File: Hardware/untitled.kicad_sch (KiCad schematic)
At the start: 3 parts, among them U1 STM32F446RET6TR

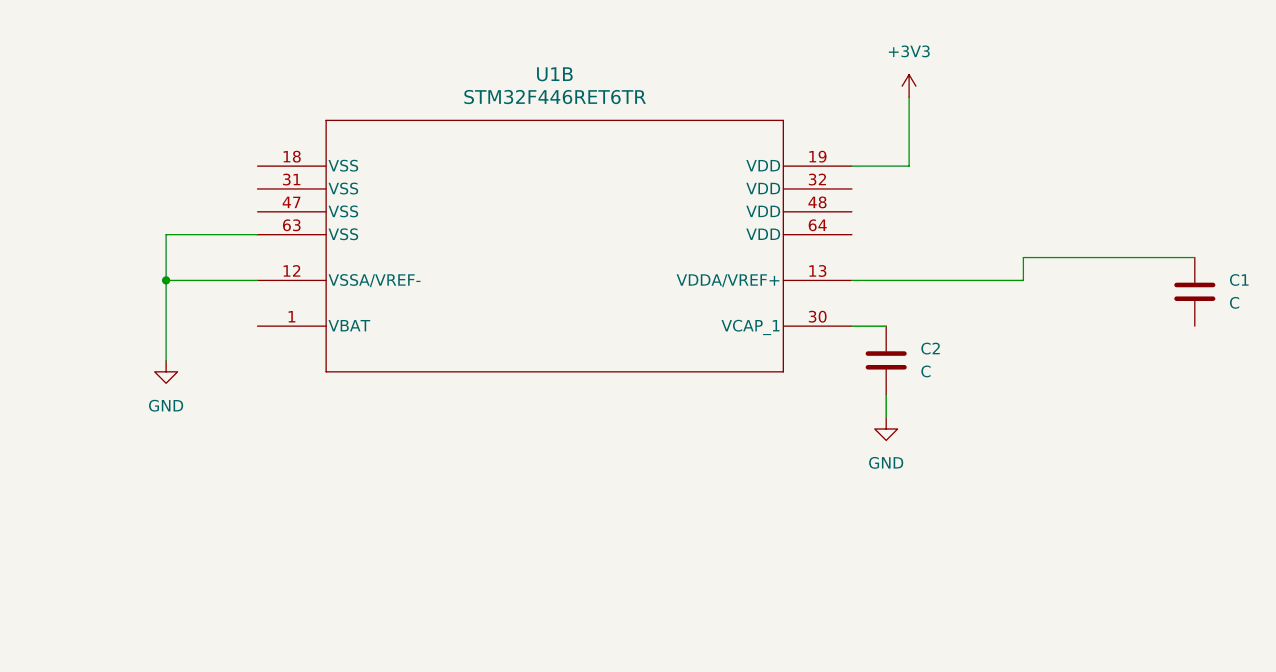
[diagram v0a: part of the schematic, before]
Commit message: Power connection touch-ups
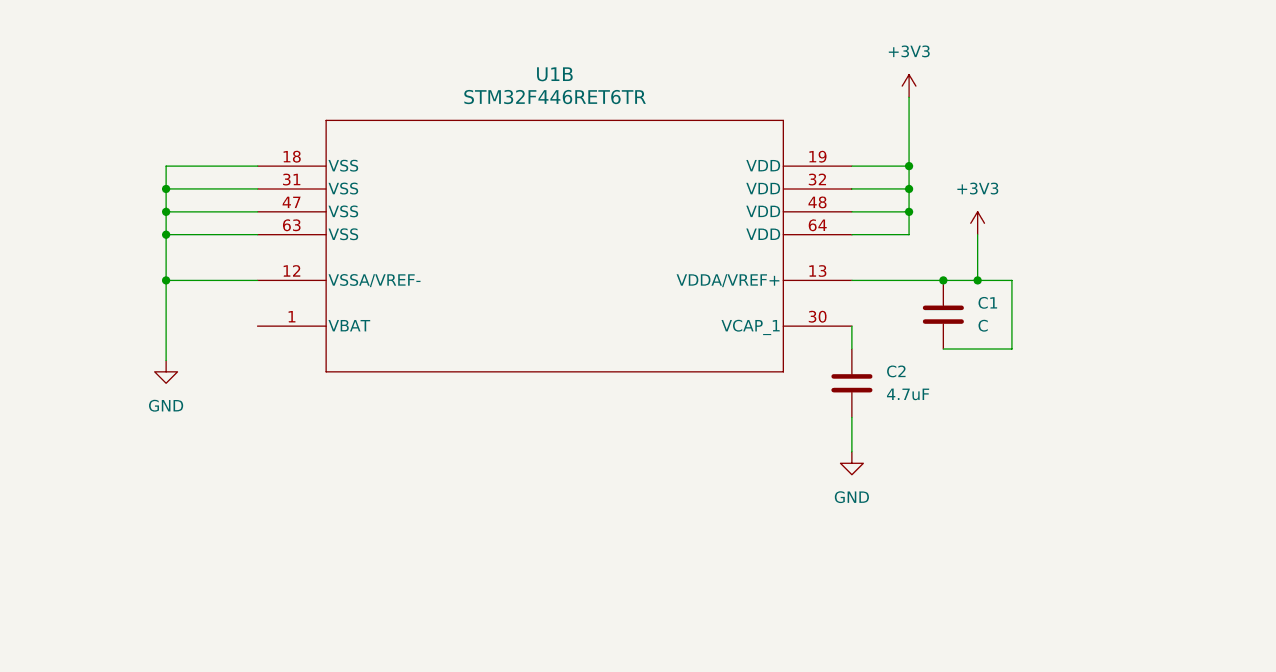
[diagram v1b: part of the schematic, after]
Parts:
- C2: value C -> 4.7uF
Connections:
- net +3V3: now also C1.1, C1.2, U1.13 (VDDA/VREF+), U1.32 (VDD), U1.48 (VDD), U1.64 (VDD)
- net GND: now also U1.18 (VSS), U1.31 (VSS), U1.47 (VSS)
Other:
- moved on the sheet: C1, C2

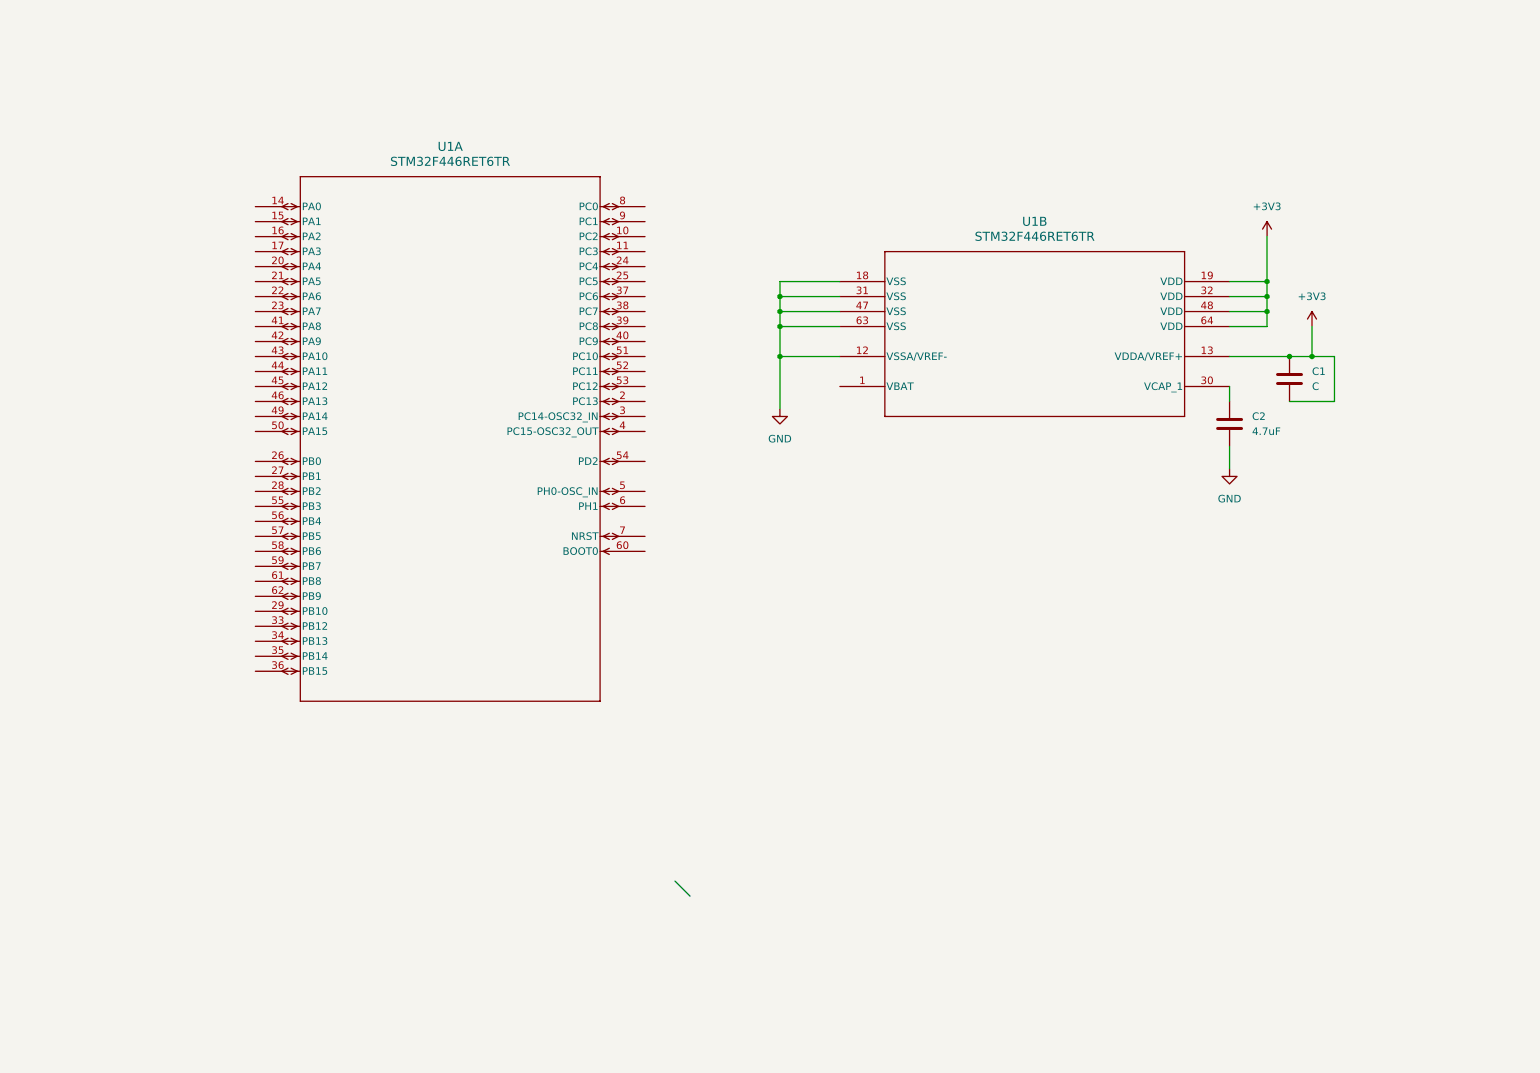
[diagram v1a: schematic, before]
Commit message: Wired the power pins + NRST + BOOT0
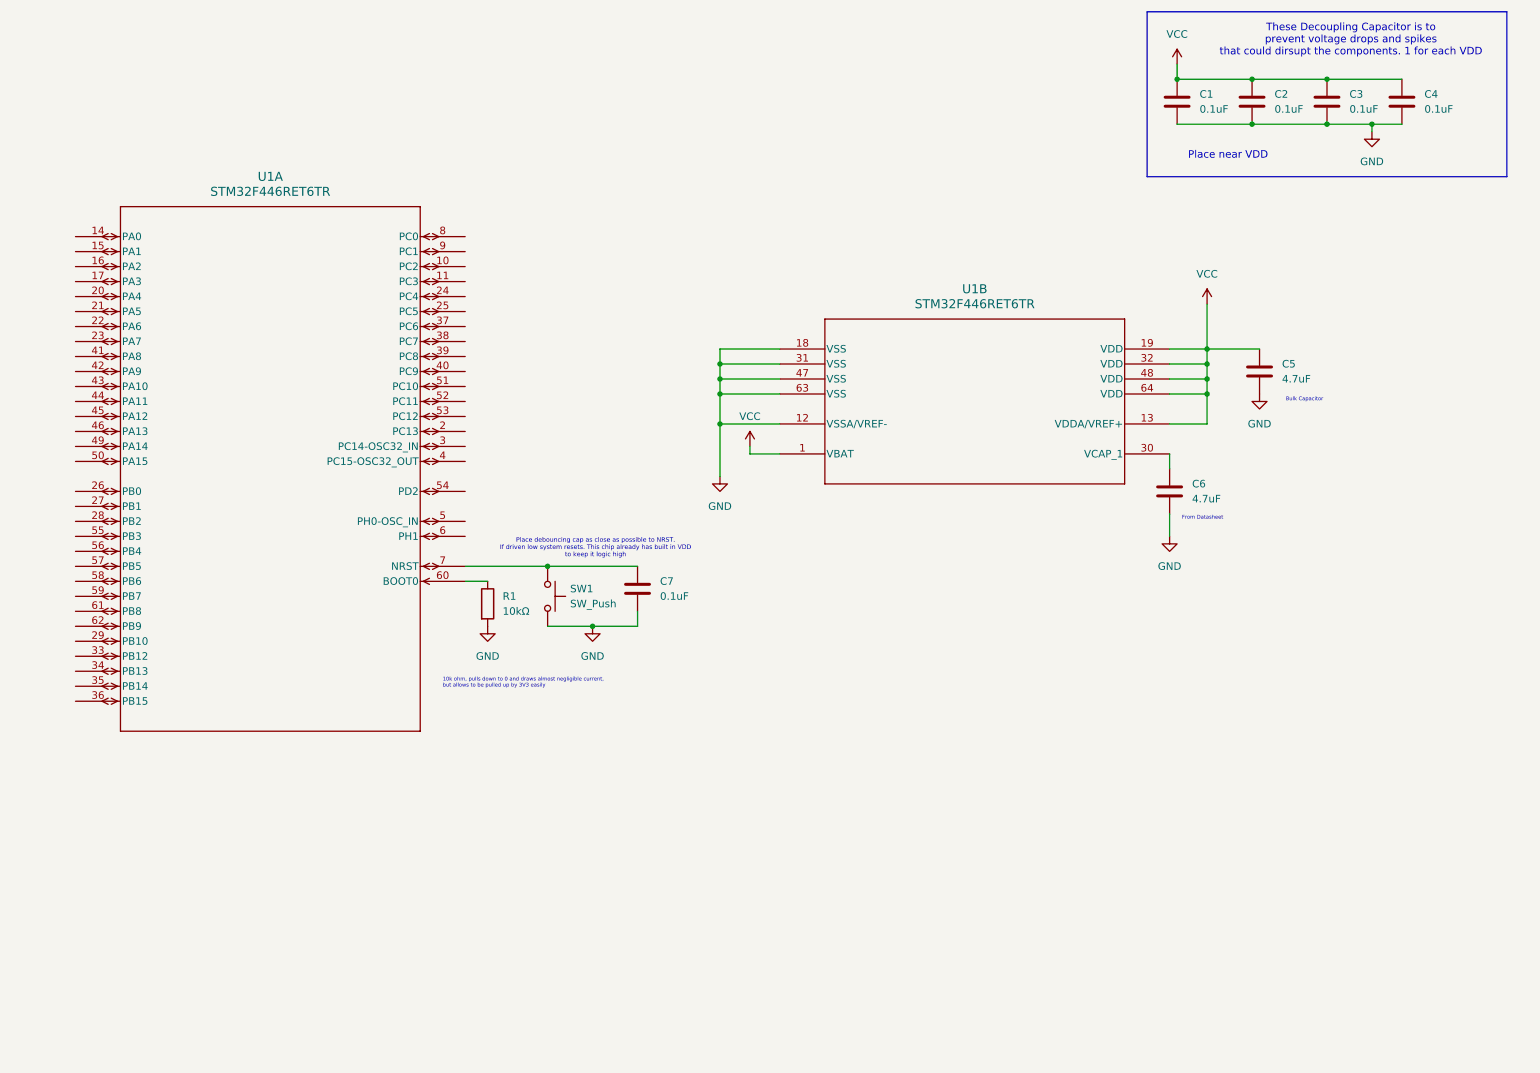
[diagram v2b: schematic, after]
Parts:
- added C2, C3, C4, C7: 0.1uF, symbol Device:C
- added C5: 4.7uF, symbol Device:C
- added R1: 10kΩ, symbol Device:R
- added SW1: SW_Push, symbol Switch:SW_Push
- C1: value C -> 0.1uF
- renumbered C2 to C6
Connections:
- net GND: now also C1.2, C2.2, C3.2, C4.2, C5.2, C7.2, R1.2, SW1.2
- net at U1.60 (BOOT0): now also R1.1
- net at U1.7 (NRST): now also C7.1, SW1.1
- net VCC: now reaches U1.1 (VBAT)
- net VCC: now also C1.1, U1.13 (VDDA/VREF+), U1.19 (VDD), U1.32 (VDD), U1.48 (VDD), U1.64 (VDD), C2.1, C3.1, C4.1, C5.1
- removed net +3V3: C1.1, C1.2, U1.13 (VDDA/VREF+), U1.19 (VDD), U1.32 (VDD), U1.48 (VDD), U1.64 (VDD)
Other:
- note added: "10k ohm, pulls down to 0 and draws almost negligible current, but allows to be pulled up by 3V3 easily"
- note added: "Bulk Capacitor"
- note added: "From Datasheet"
- note added: "Place debouncing cap as close as possible to NRST. If driven low system resets. This chip already has built in VDD to keep it logic high"
- note added: "Place near VDD"
- note added: "These Decoupling Capacitor is to prevent voltage drops and spikes that could dirsupt the components. 1 for each VDD"
- moved on the sheet: C6, U1A, U1B

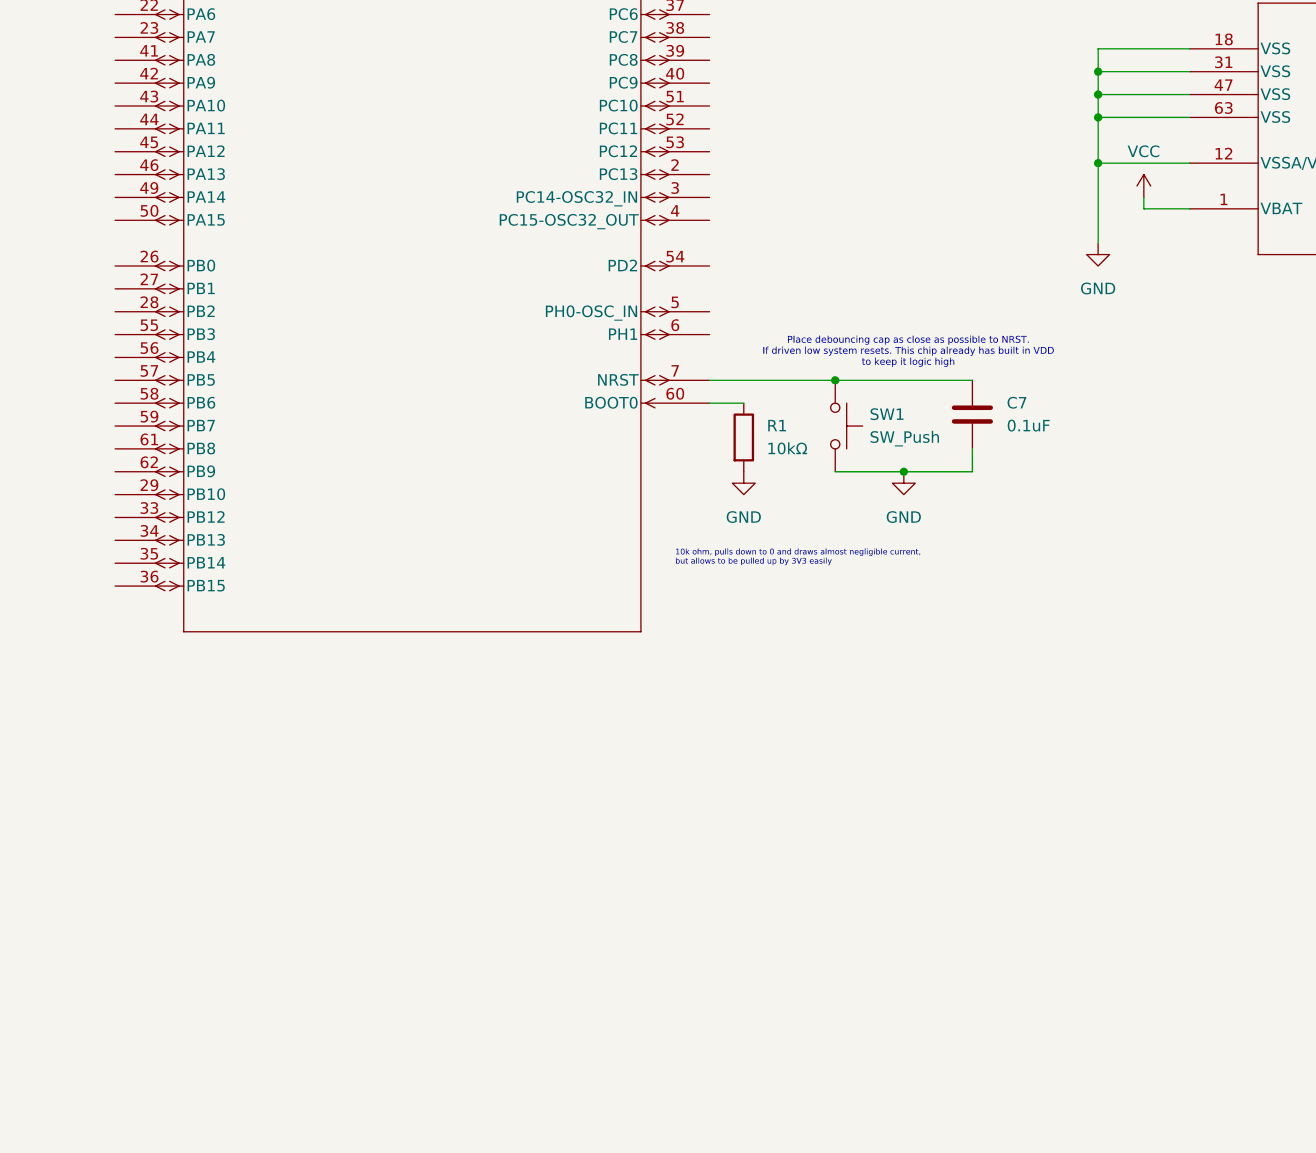
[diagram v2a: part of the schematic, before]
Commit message: Deleted a mount
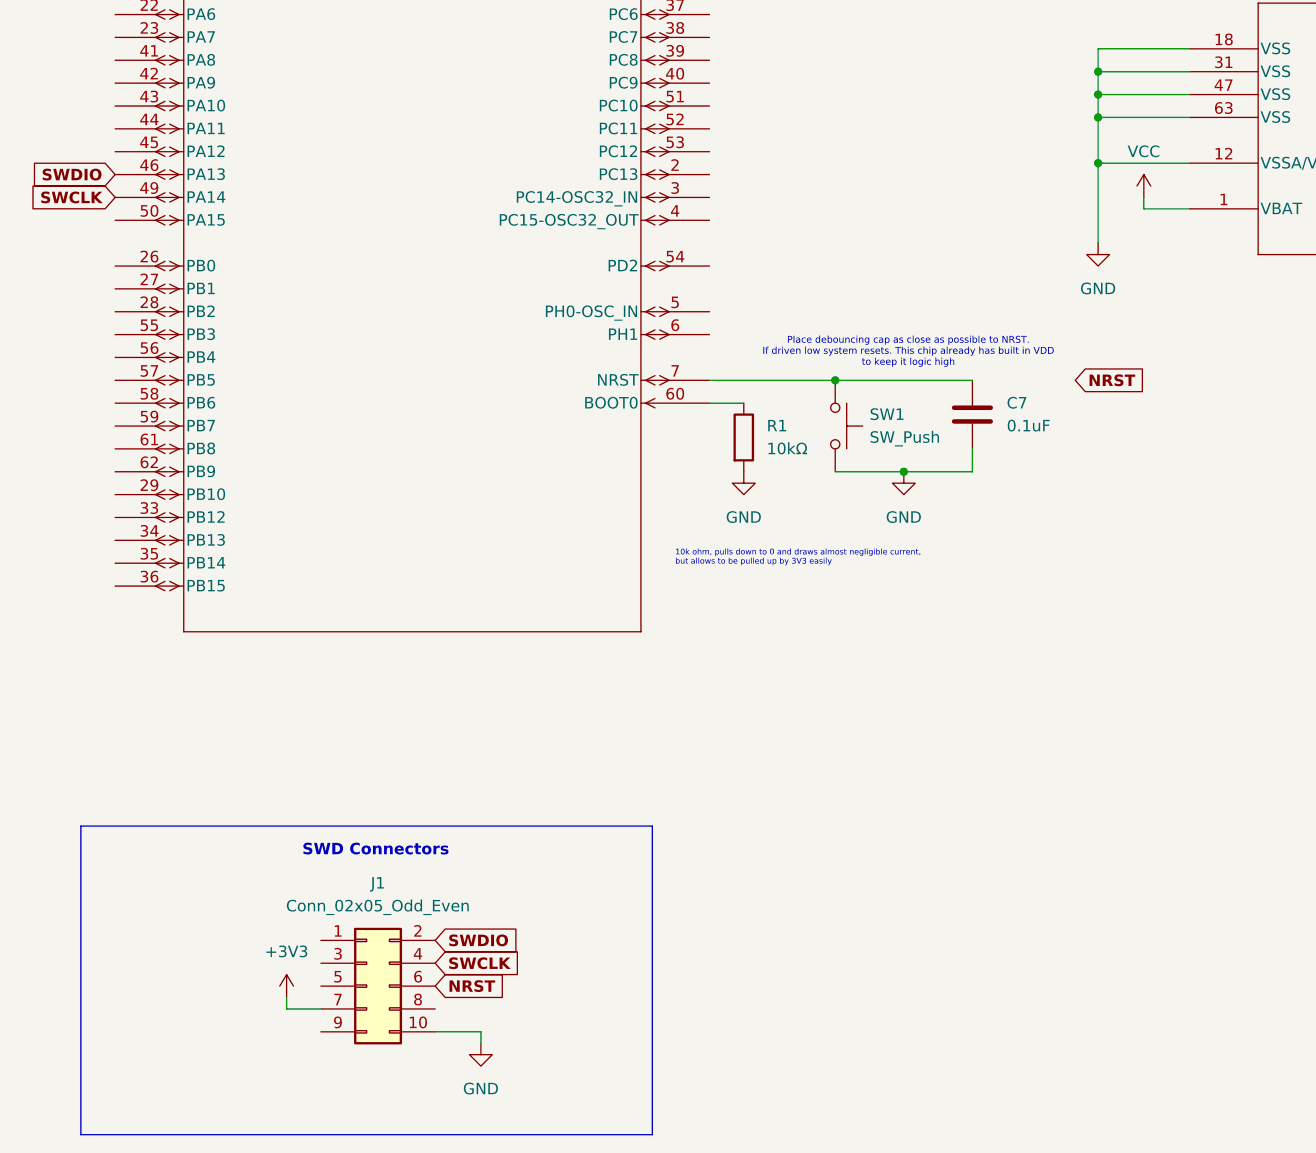
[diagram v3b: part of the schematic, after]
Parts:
- added J1: Conn_02x05_Odd_Even, symbol Connector_Generic:Conn_02x05_Odd_Even
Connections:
- net GND: now also J1.10 (Pin_10)
- net SWDIO: now reaches U1.46 (PA13)
- net SWDIO: now also J1.2 (Pin_2)
- net SWCLK: now reaches U1.49 (PA14)
- net SWCLK: now also J1.4 (Pin_4)
- new net +3V3: J1.7 (Pin_7)
- new net NRST: J1.6 (Pin_6)
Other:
- note added: "SWD Connectors"
